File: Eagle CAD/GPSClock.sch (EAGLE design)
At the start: 39 parts, among them IC3 LM1117, J1 AMP FCI 10103594-0001LF, J2 ISP, J3 POWER_JACKSUPER_BOMB_DIGITY, J4 BM06B-SRSS-TB, Q1 1A/60V/500mΩ, U1 CH340C, U3 AP2112-3.3V, U4 ATMEGA328P_TQFP, Y1 16MHz

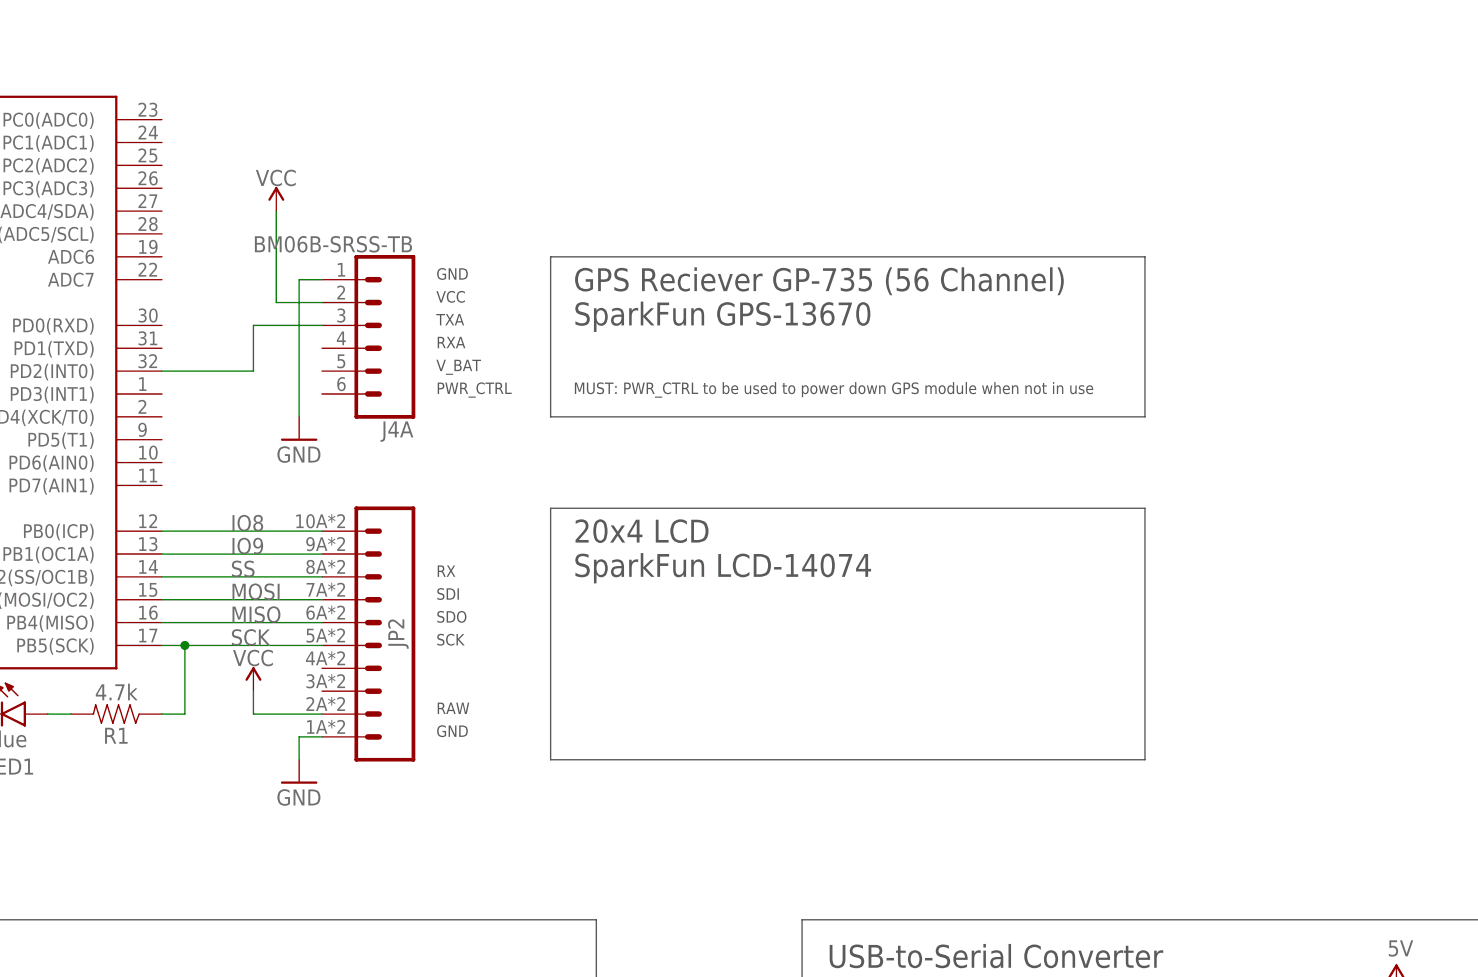
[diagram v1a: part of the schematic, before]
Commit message: updated GPS connector
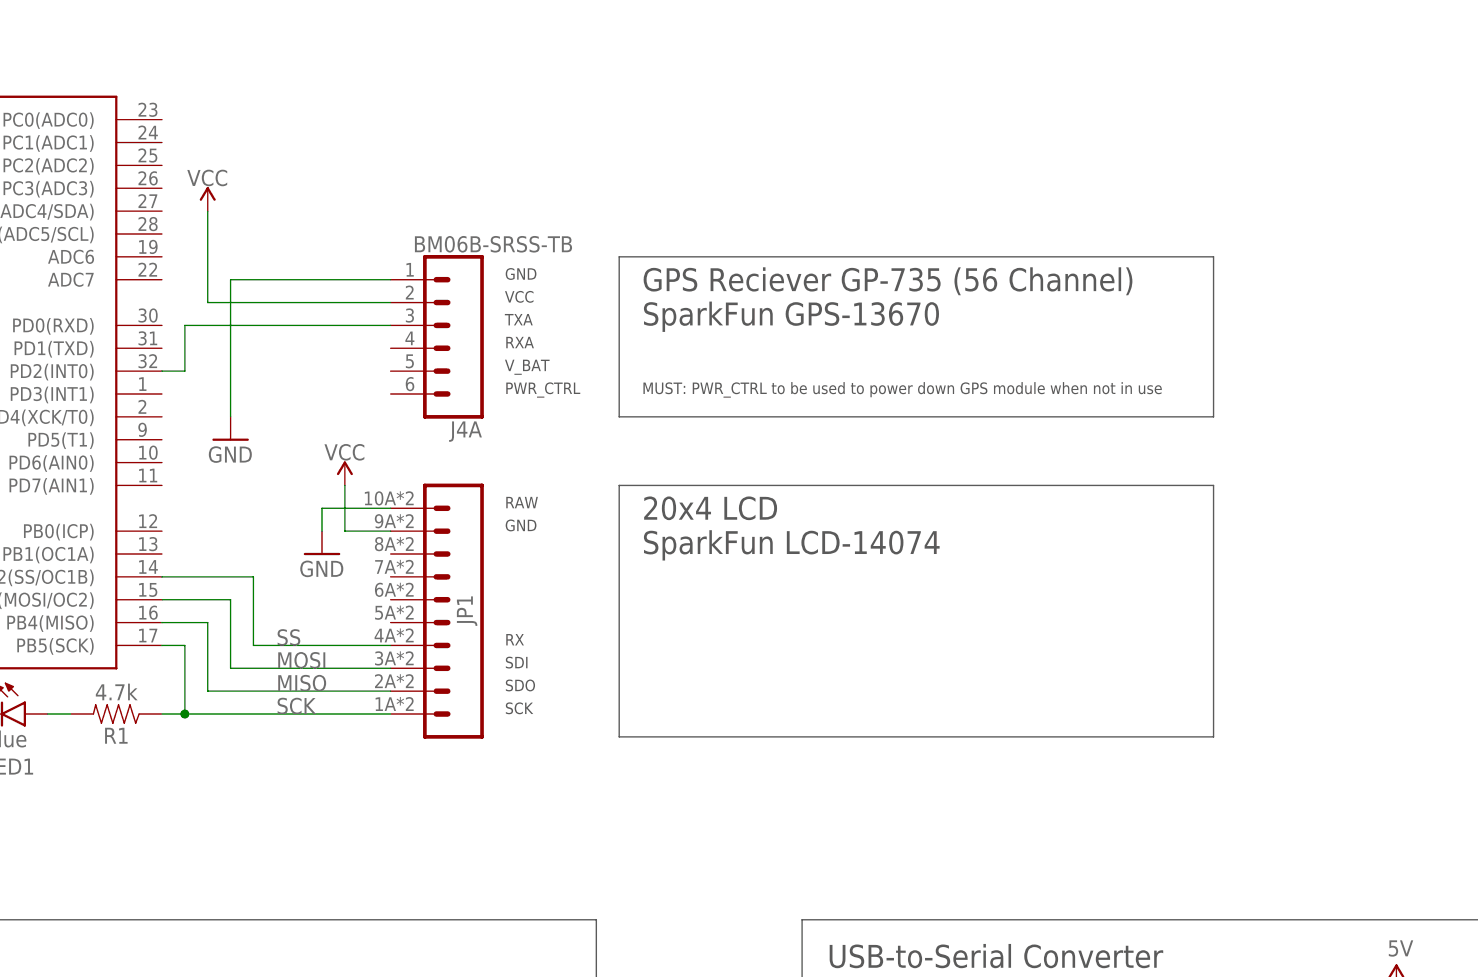
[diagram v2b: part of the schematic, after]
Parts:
- removed JP2: M10SMD_COMBO, SparkFun-Connectors:M10SMD_COMBO
- added JP1: M10SMD_COMBO, SparkFun-Connectors:M10SMD_COMBO
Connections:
- removed net IO8: JP2.10, U4.PB0(ICP)
- removed net IO9: JP2.9, U4.PB1(OC1A)
- net GND: now also JP1.10; no longer JP2.1
- net MISO: now also JP1.2; no longer JP2.6
- net MOSI: now also JP1.3; no longer JP2.7
- net SCK: now also JP1.1; no longer JP2.5
- net SS: now also JP1.4; no longer JP2.8
- net VCC: now also JP1.9; no longer JP2.2
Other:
- moved on the sheet: J4A

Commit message: Add files via upload
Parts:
- added JP2, JP3, JP4, JP5: JUMPER-SMT_2_NC_TRACE_NO-SILK, SparkFun-Jumpers:JUMPER-SMT_2_NC_TRACE_NO-SILK
- added R7: 1M, SparkFun-Resistors:1MOHM-0603-1/4W-5%
- added R8: 1k, SparkFun-Resistors:1KOHM-0603-1/10W-1%
- added TP1: TP-063, keystone:TP-063
- added U2: LIGHT_SENSORALS, SparkFun-Sensors:LIGHT_SENSORALS
- added U5: 1571984-1, TE 1571984-1:1571984-1
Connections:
- net N$7 renamed GPS_RX
- new net AMBIENT: R7.1, U2.C1, U4.PD3(INT1)
- new net DTS: R8.1, U4.PD4(XCK/T0), U5.5
- new net N$10: JP1.9, JP4.1
- new net N$11: J4A.2, JP5.1
- new net N$7: C16.1, C6.+, JP3.1, U3.OUT
- new net N$8: JP2.1, U3.EN, U3.IN
- net 5V: now also JP2.2; no longer U3.EN, U3.IN
- net GND: now also TP1.1, U2.E1, U5.1, U5.3, U5.6
- net RX-I: now also U4.PD0(RXD)
- net TX-O: now also U4.PD1(TXD)
- net VCC: now also JP3.2, JP5.2, R7.2, R8.2; no longer C16.1, C6.+, J4A.2, JP1.9, U3.OUT
- net VIN: now also JP4.2
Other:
- note added: "Daylight Savings Time"
- note removed: "Should: Alarm Circuit"
- moved on the sheet: C1, C10, C12, C15, C16, C17, C18, C2, C3, C4, C5, C6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

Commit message: Completed OSH Park's DRC
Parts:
- added C11, C13, C9: 0.1uF, SparkFun-Capacitors:0.1UF-0603-25V-(+80/-20%)
- added JP6: JUMPER-SMT_3_1-NC_TRACE_NO-SILK, SparkFun-Jumpers:JUMPER-SMT_3_1-NC_TRACE_NO-SILK
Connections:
- removed net VCC: C2.2, J2.2, JP3.2, JP5.2, R12.2, R16.2, R2.2, R3.2, R7.2, R8.2, U4.AVCC, U4.VCC@4, U4.VCC@6
- new net 3.3V: C11.2, C13.2, C2.2, J2.2, JP3.2, JP5.2, R12.2, R16.2, R2.2, R3.2, R7.2, R8.2, U4.AVCC, U4.VCC@4, U4.VCC@6
- new net N$12: C18.1, JP6.2, U1.VCC
- net 5V: now also JP6.1; no longer C18.1, U1.VCC
- net GND: now also C11.1, C13.1, C9.2
- net SHLD: now also C9.1
- net USBVCC: now also JP6.3
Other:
- note added: "Daylight Savings Time Switch"
- note added: "Team 9: Cheng, Jemmett, Jia, Liu"
- note removed: "Daylight Savings Time"
- note removed: "Does this block auto update?"
- moved on the sheet: C18, R7, U2
